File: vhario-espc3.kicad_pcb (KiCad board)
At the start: 2 copper layers, 74 x 34 mm, 57 parts, among them J1 USB_C, J2 Battery, Q1 AO3401A, Q2 2N7002, SW1 RST, SW2 DBG, SW3 PWR, SW4 PCCA, U1 cjmcu117, U2 MCP73831-2-OT, U3 espc3fn4, U4 74HC240PWR, U5 TLV75533PDBV

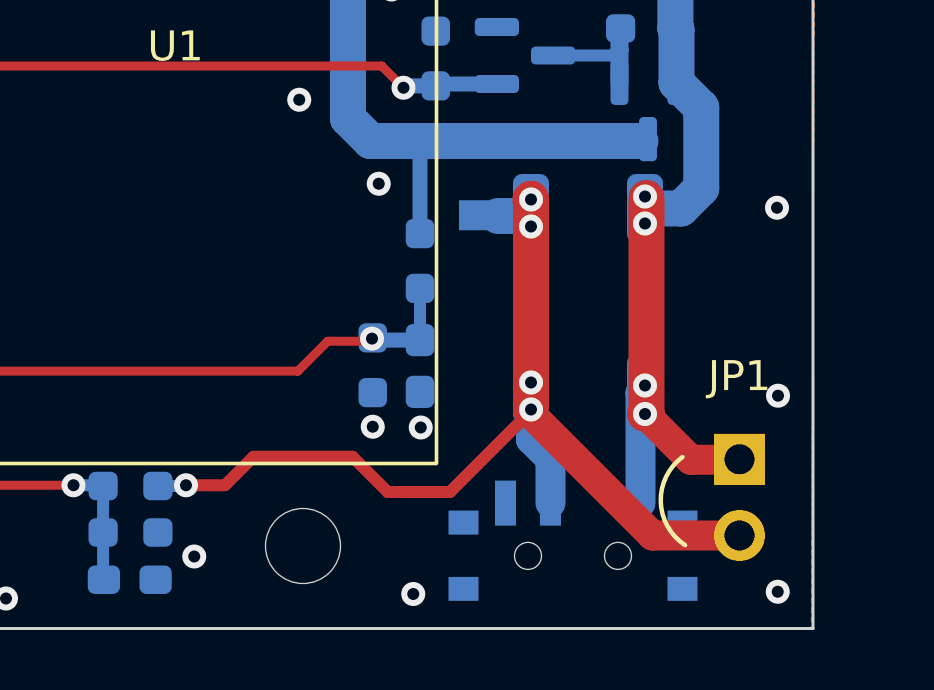
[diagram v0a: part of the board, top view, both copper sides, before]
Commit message: move via out of pad
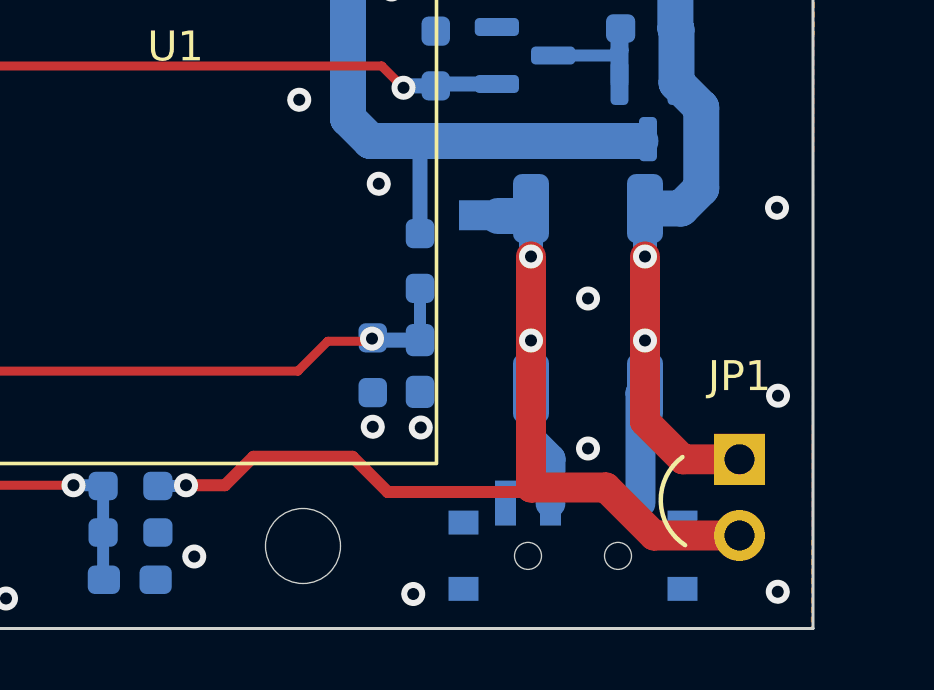
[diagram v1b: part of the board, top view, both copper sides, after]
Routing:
- net Net-(D5-Pad2): track 34.6 -> 36.3 mm, vias 5 -> 3
- net +BATT: track 81.2 -> 82.5 mm, vias 7 -> 5
- net GND: vias 81 -> 83

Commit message: optimize tracks
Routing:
- net /PWR_CTRL: track 49.1 -> 50.1 mm, vias 1 -> 3
- net /MISO: track 18.4 -> 17.8 mm
- net GND: vias 83 -> 85
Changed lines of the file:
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@@
   (segment (start 106.25 77.42) (end 106.25 76.25) (width 1) (layer "F.Cu") (net 4))
   (segment (start 96.275 86.82) (end 95.655 86.2) (width 0.6) (layer "F.Cu") (net 4))
-  (via (at 127 79.45) (size 0.8) (drill 0.4) (layers "F.Cu" "B.Cu") (free) (net 4))
+  (via (at 126.8 79.6) (size 0.8) (drill 0.4) (layers "F.Cu" "B.Cu") (free) (net 4))
   (via (at 112.625 72.6) (size 0.8) (drill 0.4) (layers "F.Cu" "B.Cu") (free) (net 4))
   (via (at 137.35 74.6) (size 0.8) (drill 0.4) (layers "F.Cu" "B.Cu") (free) (net 4))
@@
   (via (at 109.35 67.2) (size 0.8) (drill 0.4) (layers "F.Cu" "B.Cu") (free) (net 4))
   (via (at 149.925 93.3) (size 0.8) (drill 0.4) (layers "F.Cu" "B.Cu") (free) (net 4))
+  (via (at 139.1 85.2) (size 0.8) (drill 0.4) (layers "F.Cu" "B.Cu") (free) (net 4))
   (via (at 125.7 96.6) (size 0.8) (drill 0.4) (layers "F.Cu" "B.Cu") (free) (net 4))
+  (via (at 139.1 87.4) (size 0.8) (drill 0.4) (layers "F.Cu" "B.Cu") (free) (net 4))
   (via (at 148.525 85.175) (size 0.8) (drill 0.4) (layers "F.Cu" "B.Cu") (free) (net 4))
   (via (at 154.675 67.6) (size 0.8) (drill 0.4) (layers "F.Cu" "B.Cu") (free) (net 4))
@@
   (segment (start 94.23 83.25) (end 94.175 83.195) (width 0.3) (layer "F.Cu") (net 19))
   (via (at 100.25 83.25) (size 0.8) (drill 0.4) (layers "F.Cu" "B.Cu") (net 19))
-  (segment (start 156.100001 95.3) (end 157.700001 96.9) (width 1) (layer "F.Cu") (net 20))
   (segment (start 147.65 94.275) (end 148.825 95.45) (width 0.4) (layer "F.Cu") (net 20))
   (segment (start 143.4 95.225) (end 144.35 94.275) (width 0.4) (layer "F.Cu") (net 20))
+  (segment (start 154.679999 96.379999) (end 160.029999 96.379999) (width 1) (layer "F.Cu") (net 20))
   (segment (start 142.1 95.225) (end 143.4 95.225) (width 0.4) (layer "F.Cu") (net 20))
-  (segment (start 153.6 95.3) (end 156.100001 95.3) (width 1) (layer "F.Cu") (net 20))
   (segment (start 153.45 95.45) (end 153.6 95.3) (width 0.4) (layer "F.Cu") (net 20))
+  (segment (start 160.029999 96.379999) (end 160.55 96.9) (width 1) (layer "F.Cu") (net 20))
   (segment (start 144.35 94.275) (end 147.65 94.275) (width 0.4) (layer "F.Cu") (net 20))
-  (segment (start 157.700001 96.9) (end 160.55 96.9) (width 1) (layer "F.Cu") (net 20))
+  (segment (start 153.6 95.3) (end 154.679999 96.379999) (width 1) (layer "F.Cu") (net 20))
   (segment (start 148.825 95.45) (end 153.45 95.45) (width 0.4) (layer "F.Cu") (net 20))
   (segment (start 153.6 87.6) (end 153.6 90.4) (width 1) (layer "F.Cu") (net 20))
@@
   (segment (start 156.55 80.0375) (end 156.5875 80) (width 0.6) (layer "B.Cu") (net 29))
   (segment (start 156.375 80.9) (end 156.55 80.725) (width 0.4) (layer "B.Cu") (net 29))
-  (segment (start 149.35 81.975) (end 148.625 81.25) (width 0.3) (layer "F.Cu") (net 30))
-  (segment (start 148.625 81.25) (end 132 81.25) (width 0.3) (layer "F.Cu") (net 30))
-  (segment (start 132 81.25) (end 128.825 84.425) (width 0.3) (layer "F.Cu") (net 30))
-  (segment (start 128.825 84.425) (end 120.975 84.425) (width 0.3) (layer "F.Cu") (net 30))
+  (segment (start 117.97 81.42) (end 106.25 81.42) (width 0.3) (layer "F.Cu") (net 30))
   (segment (start 120.975 84.425) (end 117.97 81.42) (width 0.3) (layer "F.Cu") (net 30))
-  (segment (start 117.97 81.42) (end 106.25 81.42) (width 0.3) (layer "F.Cu") (net 30))
+  (segment (start 149.325 81.975) (end 146.9 84.4) (width 0.3) (layer "F.Cu") (net 30))
+  (segment (start 149.35 81.975) (end 149.325 81.975) (width 0.3) (layer "F.Cu") (net 30))
+  (segment (start 146.9 84.4) (end 146.7 84.6) (width 0.3) (layer "F.Cu") (net 30))
+  (segment (start 127.7 84.425) (end 120.975 84.425) (width 0.3) (layer "F.Cu") (net 30))
+  (via (at 146.7 84.6) (size 0.8) (drill 0.4) (layers "F.Cu" "B.Cu") (net 30))
+  (via (at 127.7 84.425) (size 0.8) (drill 0.4) (layers "F.Cu" "B.Cu") (net 30))
   (via (at 149.35 81.975) (size 0.8) (drill 0.4) (layers "F.Cu" "B.Cu") (net 30))
   (segment (start 152.4625 81.85) (end 150.4875 81.85) (width 0.5) (layer "B.Cu") (net 30))
+  (segment (start 145 86.3) (end 129.8 86.3) (width 0.3) (layer "B.Cu") (net 30))
   (segment (start 150.4875 81.85) (end 150.425 81.9125) (width 0.4) (layer "B.Cu") (net 30))
+  (segment (start 127.7 84.425) (end 129.575 86.3) (width 0.3) (layer "B.Cu") (net 30))
   (segment (start 150.425 81.9125) (end 149.4125 81.9125) (width 0.5) (layer "B.Cu") (net 30))
+  (segment (start 129.575 86.3) (end 129.8 86.3) (width 0.3) (layer "B.Cu") (net 30))
   (segment (start 149.4125 81.9125) (end 149.35 81.975) (width 0.4) (layer "B.Cu") (net 30))
-  (segment (start 122.25 85.42) (end 129.83 85.42) (width 0.4) (layer "F.Cu") (net 31))
-  (segment (start 130.21 85.04) (end 132.65 85.04) (width 0.4) (layer "F.Cu") (net 31))
-  (segment (start 129.83 85.42) (end 130.21 85.04) (width 0.4) (layer "F.Cu") (net 31))
+  (segment (start 146.7 84.6) (end 145 86.3) (width 0.3) (layer "B.Cu") (net 30))
+  (segment (start 129.58 85.42) (end 129.96 85.04) (width 0.4) (layer "F.Cu") (net 31))
+  (segment (start 129.96 85.04) (end 132.65 85.04) (width 0.4) (layer "F.Cu") (net 31))
   (segment (start 120.32 85.42) (end 122.25 85.42) (width 0.4) (layer "F.Cu") (net 31))
+  (segment (start 122.25 85.42) (end 129.58 85.42) (width 0.4) (layer "F.Cu") (net 31))
   (segment (start 120.3 85.4) (end 120.32 85.42) (width 0.4) (layer "F.Cu") (net 31))
   (via (at 120.3 85.4) (size 0.8) (drill 0.4) (layers "F.Cu" "B.Cu") (net 31))
@@
   (segment (start 101.3375 73.2875) (end 102.85 71.775) (width 0.4) (layer "B.Cu") (net 33))
   (segment (start 109.725 68.9875) (end 109.725 69.4625) (width 0.3) (layer "B.Cu") (net 33))
-  (segment (start 130.85 74.225) (end 131.475 73.6) (width 0.3) (layer "F.Cu") (net 34))
+  (segment (start 120.625 77.325) (end 120.625 75.375) (width 0.3) (layer "F.Cu") (net 34))
+  (segment (start 129.775 74.225) (end 130.4 73.6) (width 0.3) (layer "F.Cu") (net 34))
+  (segment (start 119.95 78) (end 120.625 77.325) (width 0.3) (layer "F.Cu") (net 34))
+  (segment (start 113.25 77.975) (end 113.275 78) (width 0.3) (layer "F.Cu") (net 34))
+  (segment (start 130.4 73.6) (end 148.25 73.6) (width 0.3) (layer "F.Cu") (net 34))
   (segment (start 120.625 75.375) (end 121.775 74.225) (width 0.3) (layer "F.Cu") (net 34))
+  (segment (start 148.25 73.6) (end 148.775 73.075) (width 0.3) (layer "F.Cu") (net 34))
+  (segment (start 121.775 74.225) (end 129.775 74.225) (width 0.3) (layer "F.Cu") (net 34))
+  (segment (start 113.25 77.975) (end 113.25 75.92) (width 0.4) (layer "F.Cu") (net 34))
   (segment (start 113.275 78) (end 119.95 78) (width 0.3) (layer "F.Cu") (net 34))
-  (segment (start 131.475 73.6) (end 148.25 73.6) (width 0.3) (layer "F.Cu") (net 34))
-  (segment (start 120.625 77.325) (end 120.625 75.375) (width 0.3) (layer "F.Cu") (net 34))
-  (segment (start 148.25 73.6) (end 148.775 73.075) (width 0.3) (layer "F.Cu") (net 34))
-  (segment (start 121.775 74.225) (end 130.85 74.225) (width 0.3) (layer "F.Cu") (net 34))
-  (segment (start 119.95 78) (end 120.625 77.325) (width 0.3) (layer "F.Cu") (net 34))
-  (segment (start 113.25 77.975) (end 113.25 75.92) (width 0.4) (layer "F.Cu") (net 34))
-  (segment (start 113.25 77.975) (end 113.275 78) (width 0.3) (layer "F.Cu") (net 34))
   (via (at 113.25 77.975) (size 0.8) (drill 0.4) (layers "F.Cu" "B.Cu") (net 34))
   (via (at 148.775 73.075) (size 0.8) (drill 0.4) (layers "F.Cu" "B.Cu") (net 34))
@@
   (segment (start 148.775 73.0825) (end 149.4175 73.725) (width 0.4) (layer "B.Cu") (net 34))
   (segment (start 149.4175 73.725) (end 149.4175 74.575) (width 0.4) (layer "B.Cu") (net 34))
-  (segment (start 122.25 79.42) (end 125.08 79.42) (width 0.4) (layer "F.Cu") (net 35))
-  (segment (start 125.08 79.42) (end 129.62 74.88) (width 0.4) (layer "F.Cu") (net 35))
-  (segment (start 129.62 74.88) (end 132.65 74.88) (width 0.4) (layer "F.Cu") (net 35))
+  (segment (start 125.58 79.42) (end 130.12 74.88) (width 0.4) (layer "F.Cu") (net 35))
+  (segment (start 122.25 79.42) (end 125.58 79.42) (width 0.4) (layer "F.Cu") (net 35))
+  (segment (start 130.12 74.88) (end 132.65 74.88) (width 0.4) (layer "F.Cu") (net 35))
   (segment (start 122.25 81.42) (end 126.33 81.42) (width 0.4) (layer "F.Cu") (net 36))
   (segment (start 126.33 81.42) (end 130.33 77.42) (width 0.4) (layer "F.Cu") (net 36))
@@
   (segment (start 130.29 79.96) (end 132.65 79.96) (width 0.4) (layer "F.Cu") (net 37))
   (segment (start 126.83 83.42) (end 130.29 79.96) (width 0.4) (layer "F.Cu") (net 37))
-  (segment (start 134.5 86.75) (end 133.67 87.58) (width 0.4) (layer "F.Cu") (net 38))
-  (segment (start 134.5 84.35) (end 134.5 86.75) (width 0.4) (layer "F.Cu") (net 38))
+  (segment (start 134.5 85.73) (end 134.5 84.35) (width 0.4) (layer "F.Cu") (net 38))
   (segment (start 124.25 89.5) (end 122.33 89.5) (width 0.4) (layer "F.Cu") (net 38))
   (segment (start 122.33 89.5) (end 122.25 89.42) (width 0.4) (layer "F.Cu") (net 38))
-  (segment (start 133.67 87.58) (end 132.65 87.58) (width 0.4) (layer "F.Cu") (net 38))
   (segment (start 132.65 87.58) (end 126.17 87.58) (width 0.4) (layer "F.Cu") (net 38))
+  (segment (start 132.65 87.58) (end 134.5 85.73) (width 0.4) (layer "F.Cu") (net 38))
   (segment (start 126.17 87.58) (end 124.25 89.5) (width 0.4) (layer "F.Cu") (net 38))
   (segment (start 132.65 82.5) (end 134.5 84.35) (width 0.4) (layer "F.Cu") (net 38))

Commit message: optimize tracks
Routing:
- net GND: vias 85 -> 89
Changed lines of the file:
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@@
   (segment (start 96.275 86.82) (end 95.655 86.2) (width 0.6) (layer "F.Cu") (net 4))
   (via (at 126.8 79.6) (size 0.8) (drill 0.4) (layers "F.Cu" "B.Cu") (free) (net 4))
+  (via (at 143 85.2) (size 0.8) (drill 0.4) (layers "F.Cu" "B.Cu") (free) (net 4))
   (via (at 112.625 72.6) (size 0.8) (drill 0.4) (layers "F.Cu" "B.Cu") (free) (net 4))
   (via (at 137.35 74.6) (size 0.8) (drill 0.4) (layers "F.Cu" "B.Cu") (free) (net 4))
   (via (at 115.8 85) (size 0.8) (drill 0.4) (layers "F.Cu" "B.Cu") (free) (net 4))
   (via (at 139.325 76.7) (size 0.8) (drill 0.4) (layers "F.Cu" "B.Cu") (free) (net 4))
+  (via (at 135.7 87.4) (size 0.8) (drill 0.4) (layers "F.Cu" "B.Cu") (free) (net 4))
   (via (at 147.4 75.05) (size 0.8) (drill 0.4) (layers "F.Cu" "B.Cu") (free) (net 4))
   (via (at 142.7 75.075) (size 0.8) (drill 0.4) (layers "F.Cu" "B.Cu") (free) (net 4))
@@
   (via (at 96.275 87.925) (size 0.8) (drill 0.4) (layers "F.Cu" "B.Cu") (free) (net 4))
   (via (at 148.95 78.7) (size 0.8) (drill 0.4) (layers "F.Cu" "B.Cu") (free) (net 4))
+  (via (at 143 87.4) (size 0.8) (drill 0.4) (layers "F.Cu" "B.Cu") (free) (net 4))
   (via (at 128.1 93.4) (size 0.8) (drill 0.4) (layers "F.Cu" "B.Cu") (free) (net 4))
   (via (at 155.5 94) (size 0.8) (drill 0.4) (layers "F.Cu" "B.Cu") (free) (net 4))
@@
   (via (at 161.8 85.975) (size 0.8) (drill 0.4) (layers "F.Cu" "B.Cu") (free) (net 4))
   (via (at 120.525 69.925) (size 0.8) (drill 0.4) (layers "F.Cu" "B.Cu") (free) (net 4))
+  (via (at 135.7 85.2) (size 0.8) (drill 0.4) (layers "F.Cu" "B.Cu") (free) (net 4))
   (via (at 161.79162 77.913961) (size 0.8) (drill 0.4) (layers "F.Cu" "B.Cu") (free) (net 4))
   (via (at 104.725 77.425) (size 0.8) (drill 0.4) (layers "F.Cu" "B.Cu") (net 4))
@@
   (segment (start 156.55 80.0375) (end 156.5875 80) (width 0.6) (layer "B.Cu") (net 29))
   (segment (start 156.375 80.9) (end 156.55 80.725) (width 0.4) (layer "B.Cu") (net 29))
+  (segment (start 149.325 81.975) (end 149.35 81.975) (width 0.3) (layer "F.Cu") (net 30))
   (segment (start 117.97 81.42) (end 106.25 81.42) (width 0.3) (layer "F.Cu") (net 30))
+  (segment (start 145.9 85.4) (end 149.325 81.975) (width 0.3) (layer "F.Cu") (net 30))
   (segment (start 120.975 84.425) (end 117.97 81.42) (width 0.3) (layer "F.Cu") (net 30))
-  (segment (start 149.325 81.975) (end 146.9 84.4) (width 0.3) (layer "F.Cu") (net 30))
-  (segment (start 149.35 81.975) (end 149.325 81.975) (width 0.3) (layer "F.Cu") (net 30))
-  (segment (start 146.9 84.4) (end 146.7 84.6) (width 0.3) (layer "F.Cu") (net 30))
   (segment (start 127.7 84.425) (end 120.975 84.425) (width 0.3) (layer "F.Cu") (net 30))
-  (via (at 146.7 84.6) (size 0.8) (drill 0.4) (layers "F.Cu" "B.Cu") (net 30))
+  (via (at 145.9 85.4) (size 0.8) (drill 0.4) (layers "F.Cu" "B.Cu") (net 30))
   (via (at 127.7 84.425) (size 0.8) (drill 0.4) (layers "F.Cu" "B.Cu") (net 30))
   (via (at 149.35 81.975) (size 0.8) (drill 0.4) (layers "F.Cu" "B.Cu") (net 30))
+  (segment (start 145 86.3) (end 129.575 86.3) (width 0.3) (layer "B.Cu") (net 30))
   (segment (start 152.4625 81.85) (end 150.4875 81.85) (width 0.5) (layer "B.Cu") (net 30))
-  (segment (start 145 86.3) (end 129.8 86.3) (width 0.3) (layer "B.Cu") (net 30))
+  (segment (start 145.9 85.4) (end 145 86.3) (width 0.3) (layer "B.Cu") (net 30))
+  (segment (start 129.575 86.3) (end 127.7 84.425) (width 0.3) (layer "B.Cu") (net 30))
   (segment (start 150.4875 81.85) (end 150.425 81.9125) (width 0.4) (layer "B.Cu") (net 30))
-  (segment (start 127.7 84.425) (end 129.575 86.3) (width 0.3) (layer "B.Cu") (net 30))
   (segment (start 150.425 81.9125) (end 149.4125 81.9125) (width 0.5) (layer "B.Cu") (net 30))
-  (segment (start 129.575 86.3) (end 129.8 86.3) (width 0.3) (layer "B.Cu") (net 30))
   (segment (start 149.4125 81.9125) (end 149.35 81.975) (width 0.4) (layer "B.Cu") (net 30))
-  (segment (start 146.7 84.6) (end 145 86.3) (width 0.3) (layer "B.Cu") (net 30))
   (segment (start 129.58 85.42) (end 129.96 85.04) (width 0.4) (layer "F.Cu") (net 31))
   (segment (start 129.96 85.04) (end 132.65 85.04) (width 0.4) (layer "F.Cu") (net 31))
